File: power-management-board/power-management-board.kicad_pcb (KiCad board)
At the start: 2 copper layers, 90 x 70 mm, 127 parts, among them IC1 LM74502QDDFRQ1, IC2 TLP7820_TP4,E, IC3 MCP2562, J1 Conn_01x02, J2 Conn_01x02, J3 Conn_01x04, J4 Conn_01x04, J5 Conn_01x04_Pin, J6 Conn_01x02_Pin, J7 Conn_01x02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

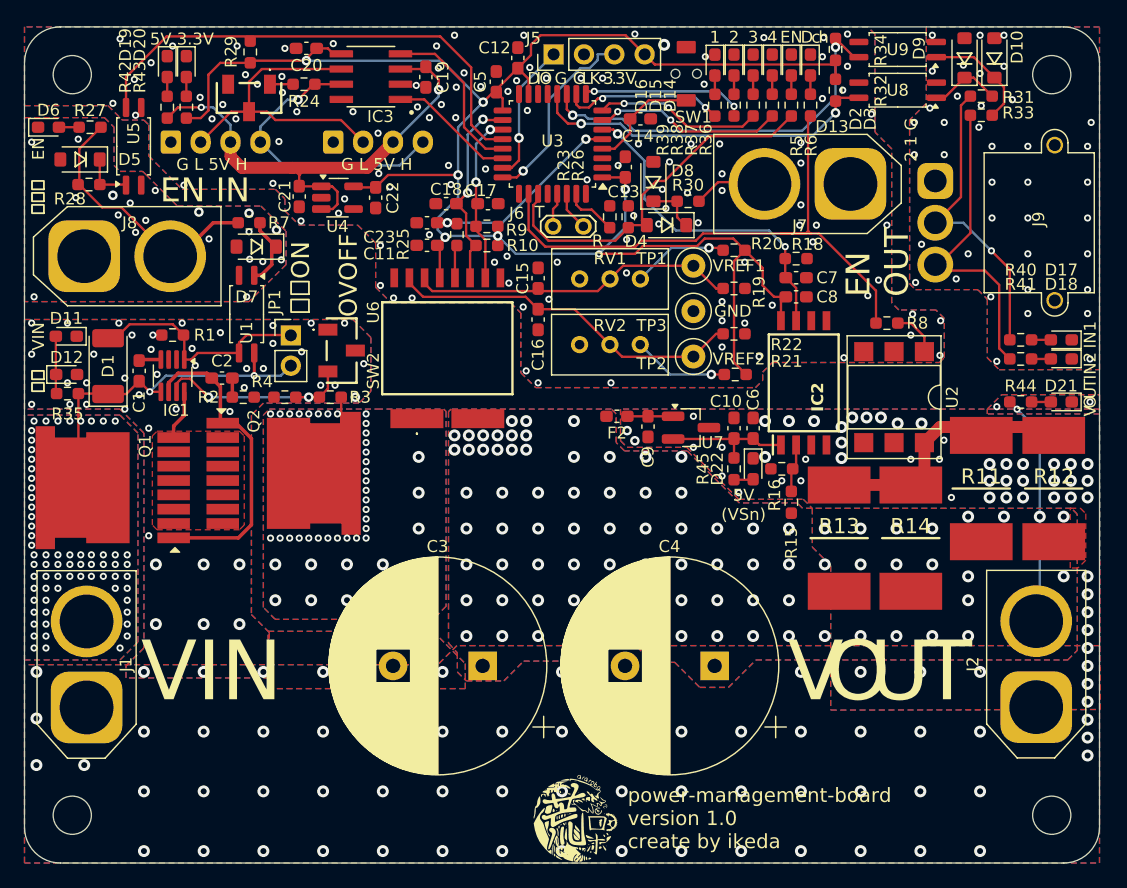
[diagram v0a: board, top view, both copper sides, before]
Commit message: fix:わかりにくいリファレンス番号を消し、OVOFFなどパット見でわからない言葉を一般化、シルクの隙間を作り可読性向上
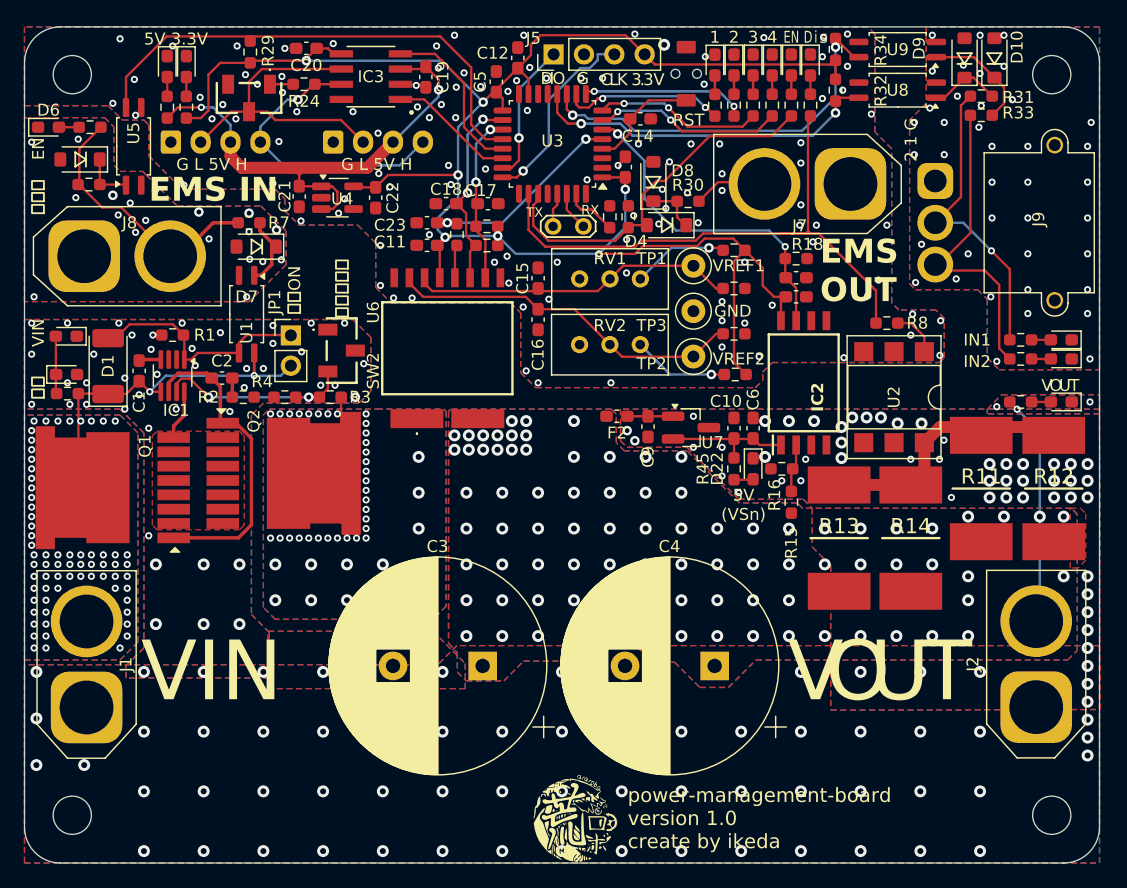
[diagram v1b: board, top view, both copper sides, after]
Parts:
- renumbered SW1 to RST
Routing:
- net GNDD: vias 113 -> 112
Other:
- board text added: "EMS IN"
- board text added: "EMS OUT"
- board text added: "RX"
- board text added: "TX"
- board text added: "i"
- board text added: "s"
- board text added: "過電圧保護"
- board text removed: "EN IN"
- board text removed: "EN OUT"
- board text removed: "OVOFF"
- board text removed: "R"
- board text removed: "c"
- board text removed: "h"
